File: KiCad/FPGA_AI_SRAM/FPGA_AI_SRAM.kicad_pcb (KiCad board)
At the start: 2 copper layers, 0 parts

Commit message: paddle schematic done
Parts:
- added C1: 0.1uF, Capacitor_SMD:C_0805_2012Metric, B.Cu at (130.8, 45.7)
- added J1: Conn_01x22_Male, Connector_PinHeader_2.54mm:PinHeader_1x22_P2.54mm_Vertical, F.Cu at (127.0, 59.7)
- added J2: Conn_01x22_Male, Connector_PinHeader_2.54mm:PinHeader_1x22_P2.54mm_Vertical, F.Cu at (134.6, 59.7)
- added U1: CY62157, Package_SO:TSOP-I-48_18.4x12mm_P0.5mm, F.Cu at (130.8, 45.7)

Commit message: possible pcb v1
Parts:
- C1: moved to F.Cu
- moved U1 45.4 mm to (110.5, 86.4)
- moved C1 36.9 mm to (106.7, 73.7)
- moved J1 25.4 mm to (101.6, 59.7)
- moved J2 15.2 mm to (119.4, 59.7)
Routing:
- net Net-(J1-Pad2): track 0.00 -> 60.4 mm
- net Net-(J2-Pad15): track 0.00 -> 57.0 mm
- net Net-(J1-Pad20): track 0.00 -> 44.0 mm
- net Net-(J2-Pad22): track 0.00 -> 40.4 mm, vias 0 -> 1
- net Net-(J1-Pad21): track 0.00 -> 40.1 mm, vias 0 -> 1
- net Net-(J1-Pad3): track 0.00 -> 37.5 mm, vias 0 -> 1
- net Net-(J2-Pad21): track 0.00 -> 37.2 mm, vias 0 -> 1
- net Net-(J1-Pad5): track 0.00 -> 36.3 mm, vias 0 -> 1
- net ~BLE: track 0.00 -> 36.1 mm
- net Net-(J2-Pad20): track 0.00 -> 35.6 mm, vias 0 -> 1
- net Net-(J1-Pad4): track 0.00 -> 34.5 mm, vias 0 -> 1
- net ~BHE: track 0.00 -> 33.5 mm
- net Net-(J2-Pad19): track 0.00 -> 32.4 mm, vias 0 -> 1
- net Net-(J2-Pad18): track 0.00 -> 30.3 mm, vias 0 -> 1
- net Net-(J1-Pad6): track 0.00 -> 29.0 mm, vias 0 -> 1
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- added copper zone on B.Cu, net GND
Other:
- board outline added: 22.9 x 58.4 mm
- board text added: "1 4"
- board text added: "10"
- board text added: "11"
- board text added: "12"
- board text added: "13"
- board text added: "3V3"
- board text added: "5"
- board text added: "6"
- board text added: "7"
- board text added: "8"
- board text added: "8Mbit SRAM"
- board text added: "9"
- board text added: "A0"
- board text added: "A1"
- board text added: "A15"
- board text added: "A16"
- board text added: "A17"
- board text added: "A18"
- board text added: "A19"
- board text added: "A2"
- board text added: "A3"
- board text added: "A4"
- board text added: "CE2"
- board text added: "D0"
- board text added: "D1"
- board text added: "D2"
- board text added: "D3"
- board text added: "D4"
- board text added: "D5"
- board text added: "D6"
- board text added: "GND"
- board text added: "~BHE"
- board text added: "~BLE"
- board text added: "~BYTE"
- board text added: "~CE1"
- board text added: "~OE"
- board text added: "~WE"

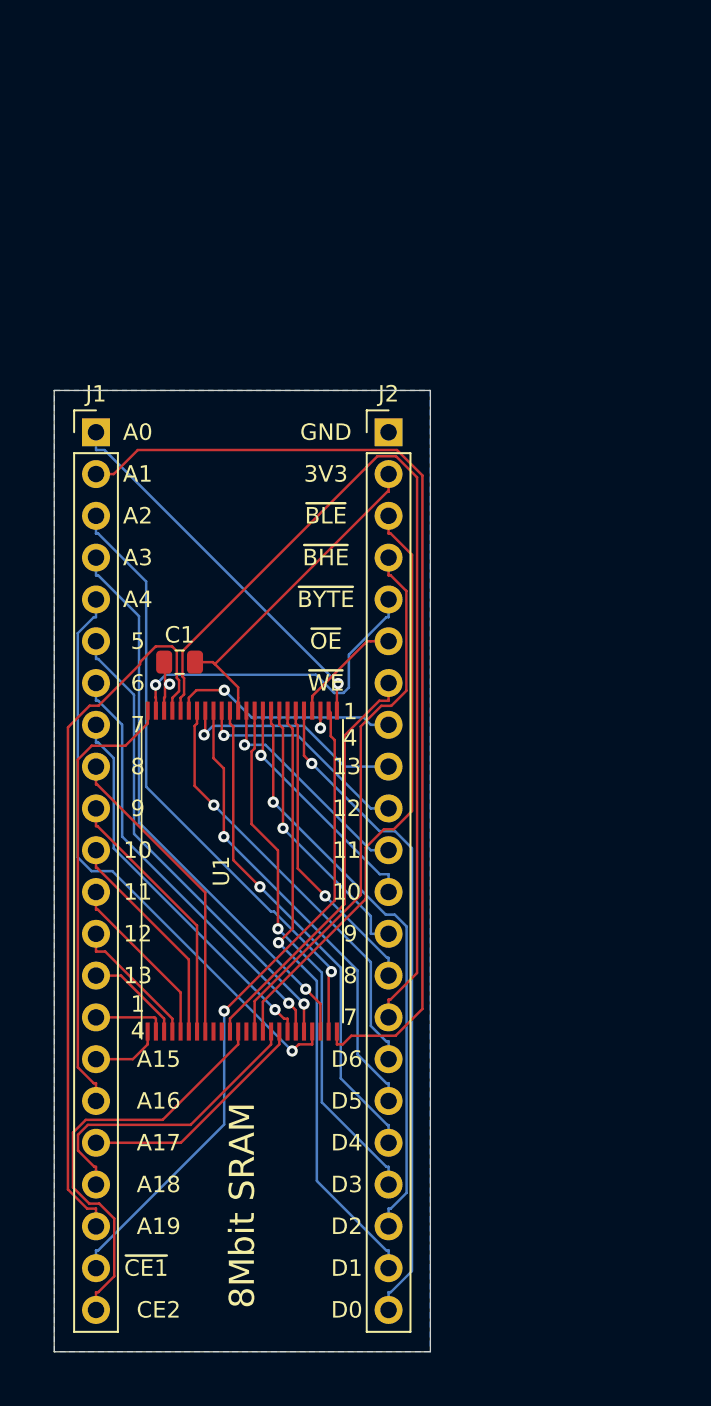
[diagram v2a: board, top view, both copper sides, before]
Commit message: better board with hand routed decoupler
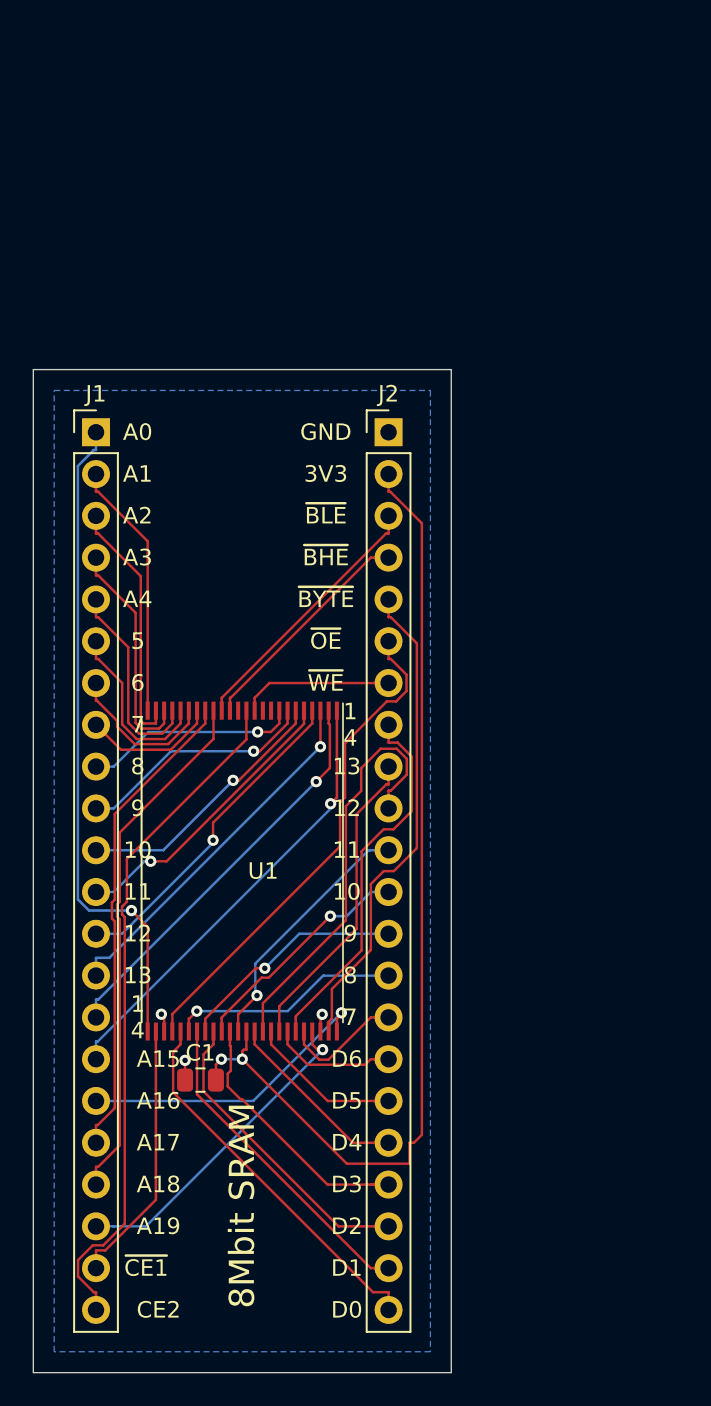
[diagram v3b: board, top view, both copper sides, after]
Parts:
- moved C1 25.4 mm to (108.0, 99.1)
- turned U1 to 270 degrees
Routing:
- net Net-(J2-Pad15): track 57.0 -> 7.37 mm
- net Net-(J1-Pad2): track 60.4 -> 15.8 mm
- net +3V3: track 20.6 -> 60.6 mm, vias 0 -> 2
- net Net-(J1-Pad20): track 44.0 -> 19.8 mm, vias 0 -> 1
- net Net-(J1-Pad5): track 36.3 -> 12.4 mm, vias 1 -> 0
- net Net-(J1-Pad21): track 40.1 -> 16.2 mm, vias 1 -> 0
- net ~OE: track 6.91 -> 30.5 mm
- net Net-(J1-Pad16): track 4.29 -> 27.3 mm, vias 0 -> 1
- net Net-(J1-Pad3): track 37.5 -> 15.4 mm, vias 1 -> 0
- net Net-(J1-Pad4): track 34.5 -> 13.9 mm, vias 1 -> 0
- net Net-(J1-Pad15): track 4.45 -> 24.6 mm, vias 0 -> 1
- net ~BLE: track 36.1 -> 16.1 mm
- net ~BHE: track 33.5 -> 13.9 mm
- net Net-(J2-Pad18): track 30.3 -> 11.4 mm, vias 1 -> 0
- net Net-(J2-Pad17): track 28.2 -> 9.34 mm, vias 1 -> 0
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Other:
- board size 22.9 x 58.4 mm -> 25.4 x 61 mm

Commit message: better board fully autorouted
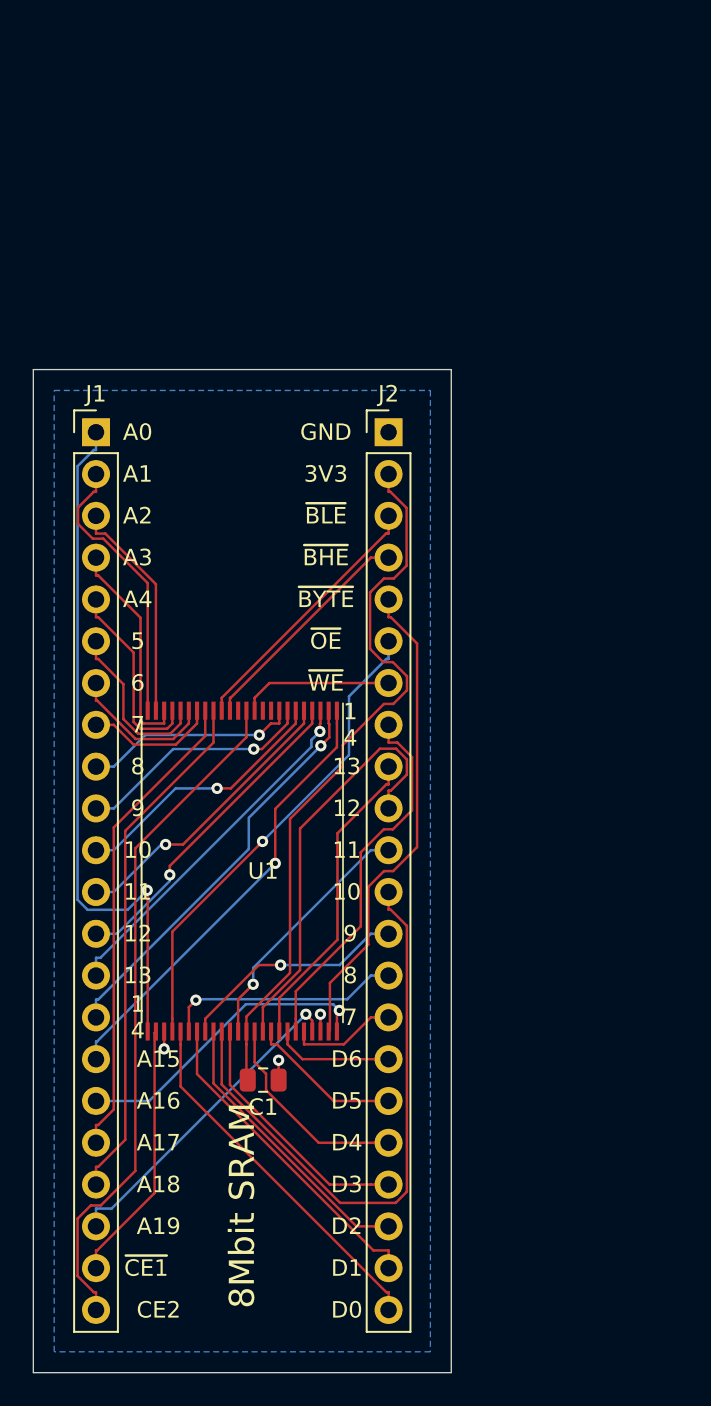
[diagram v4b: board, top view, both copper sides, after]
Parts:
- moved C1 3.81 mm to (111.8, 99.1), turned to 180 degrees
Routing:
- net Net-(J2-Pad12): track 14.2 -> 36.5 mm, vias 1 -> 0
- net +3V3: track 60.6 -> 44.3 mm, vias 2 -> 0
- net Net-(J1-Pad1): track 40.2 -> 42.5 mm
- net Net-(J1-Pad3): track 15.4 -> 13.7 mm
- net Net-(J2-Pad19): track 16.8 -> 15.4 mm
- net Net-(J1-Pad2): track 15.8 -> 17.0 mm
- net ~OE: track 30.5 -> 29.2 mm, vias 0 -> 1
- net Net-(J2-Pad18): track 11.4 -> 12.6 mm
- net Net-(J2-Pad20): track 18.5 -> 17.4 mm
- net Net-(J2-Pad22): track 23.1 -> 22.2 mm
- net Net-(J2-Pad15): track 7.37 -> 6.60 mm
- net Net-(J1-Pad4): track 13.9 -> 13.4 mm
- net Net-(J1-Pad6): track 10.9 -> 10.4 mm

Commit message: improved silkscreen, added 3d img
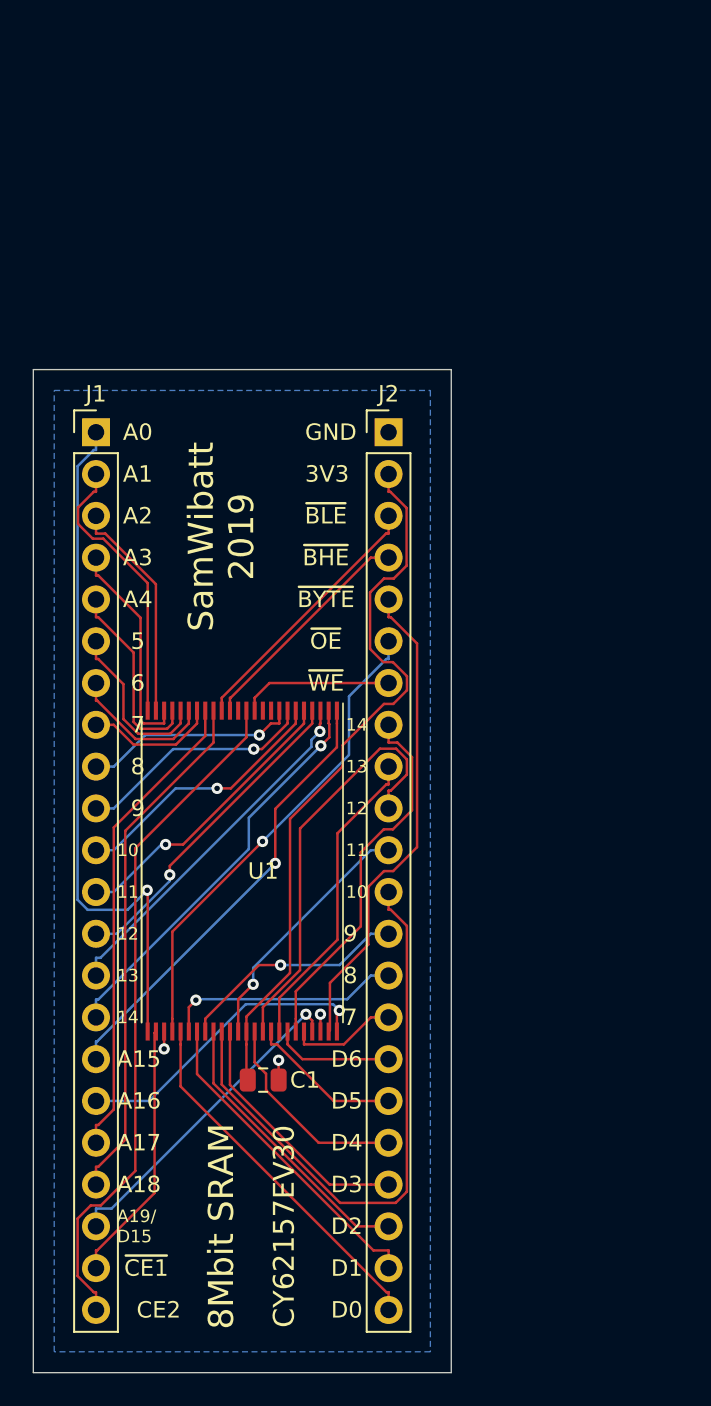
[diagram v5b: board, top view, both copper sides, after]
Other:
- board text added: "14"
- board text added: "A19/ D15"
- board text added: "CY62157EV30"
- board text added: "SamWibatt 2019"
- board text removed: "1 4"
- board text removed: "A19"
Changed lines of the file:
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@@
   (general
     (thickness 1.6)
-    (drawings 49)
+    (drawings 51)
     (tracks 309)
     (zones 0)
@@
     (tags capacitor)
     (attr smd)
-    (fp_text reference C1 (at 0 -1.65) (layer F.SilkS)
+    (fp_text reference C1 (at -2.54 0) (layer F.SilkS)
       (effects (font (size 1 1) (thickness 0.15)))
     )
@@
     )
   )
-  (gr_text "8Mbit SRAM" (at 110.49 106.68 90) (layer F.SilkS)
+  (gr_text "SamWibatt\n2019" (at 109.22 66.04 90) (layer F.SilkS)
+    (effects (font (size 1.524 1.524) (thickness 0.15)))
+  )
+  (gr_text CY62157EV30 (at 113.03 107.95 90) (layer F.SilkS)
+    (effects (font (size 1.27 1.27) (thickness 0.15)))
+  )
+  (gr_text "8Mbit SRAM" (at 109.22 107.95 90) (layer F.SilkS)
     (effects (font (size 1.524 1.524) (thickness 0.15)))
   )
@@
     (effects (font (size 1 1) (thickness 0.15)) (justify left))
   )
-  (gr_text "A19 " (at 105.41 107.95) (layer F.SilkS)
-    (effects (font (size 1 1) (thickness 0.15)))
-  )
-  (gr_text "A18 " (at 105.41 105.41) (layer F.SilkS)
-    (effects (font (size 1 1) (thickness 0.15)))
-  )
-  (gr_text "A17 " (at 105.41 102.87) (layer F.SilkS)
-    (effects (font (size 1 1) (thickness 0.15)))
-  )
-  (gr_text "A16 " (at 105.41 100.33) (layer F.SilkS)
-    (effects (font (size 1 1) (thickness 0.15)))
-  )
-  (gr_text "1 \n4 " (at 104.14 95.25) (layer F.SilkS)
-    (effects (font (size 1 1) (thickness 0.15)))
-  )
-  (gr_text "A15 " (at 105.41 97.79) (layer F.SilkS)
-    (effects (font (size 1 1) (thickness 0.15)))
-  )
-  (gr_text "13 " (at 104.14 92.71) (layer F.SilkS)
-    (effects (font (size 1 1) (thickness 0.15)))
-  )
-  (gr_text "12 " (at 104.14 90.17) (layer F.SilkS)
-    (effects (font (size 1 1) (thickness 0.15)))
-  )
-  (gr_text "11 " (at 104.14 87.63) (layer F.SilkS)
-    (effects (font (size 1 1) (thickness 0.15)))
-  )
-  (gr_text "10 " (at 104.14 85.09) (layer F.SilkS)
-    (effects (font (size 1 1) (thickness 0.15)))
+  (gr_text "A19/\nD15" (at 102.87 107.95) (layer F.SilkS)
+    (effects (font (size 0.762 0.762) (thickness 0.15)) (justify left))
+  )
+  (gr_text A18 (at 102.87 105.41) (layer F.SilkS)
+    (effects (font (size 1 1) (thickness 0.15)) (justify left))
+  )
+  (gr_text A17 (at 102.87 102.87) (layer F.SilkS)
+    (effects (font (size 1 1) (thickness 0.15)) (justify left))
+  )
+  (gr_text A16 (at 102.87 100.33) (layer F.SilkS)
+    (effects (font (size 1 1) (thickness 0.15)) (justify left))
+  )
+  (gr_text 14 (at 102.87 95.25) (layer F.SilkS)
+    (effects (font (size 0.762 0.762) (thickness 0.15)) (justify left))
+  )
+  (gr_text A15 (at 102.87 97.79) (layer F.SilkS)
+    (effects (font (size 1 1) (thickness 0.15)) (justify left))
+  )
+  (gr_text 13 (at 102.87 92.71) (layer F.SilkS)
+    (effects (font (size 0.762 0.762) (thickness 0.15)) (justify left))
+  )
+  (gr_text 12 (at 102.87 90.17) (layer F.SilkS)
+    (effects (font (size 0.762 0.762) (thickness 0.15)) (justify left))
+  )
+  (gr_text 11 (at 102.87 87.63) (layer F.SilkS)
+    (effects (font (size 0.762 0.762) (thickness 0.15)) (justify left))
+  )
+  (gr_text 10 (at 102.87 85.09) (layer F.SilkS)
+    (effects (font (size 0.762 0.762) (thickness 0.15)) (justify left))
   )
   (gr_text "9 " (at 104.14 82.55) (layer F.SilkS)
@@
     (effects (font (size 1 1) (thickness 0.15)))
   )
-  (gr_text " 1\n 4" (at 116.84 77.47) (layer F.SilkS)
-    (effects (font (size 1 1) (thickness 0.15)))
-  )
-  (gr_text 13 (at 116.84 80.01) (layer F.SilkS)
-    (effects (font (size 1 1) (thickness 0.15)))
-  )
-  (gr_text 12 (at 116.84 82.55) (layer F.SilkS)
-    (effects (font (size 1 1) (thickness 0.15)))
-  )
-  (gr_text 11 (at 116.84 85.09) (layer F.SilkS)
-    (effects (font (size 1 1) (thickness 0.15)))
-  )
-  (gr_text 10 (at 116.84 87.63) (layer F.SilkS)
-    (effects (font (size 1 1) (thickness 0.15)))
+  (gr_text 14 (at 118.11 77.47) (layer F.SilkS)
+    (effects (font (size 0.762 0.762) (thickness 0.15)) (justify right))
+  )
+  (gr_text 13 (at 118.11 80.01) (layer F.SilkS)
+    (effects (font (size 0.762 0.762) (thickness 0.15)) (justify right))
+  )
+  (gr_text 12 (at 118.11 82.55) (layer F.SilkS)
+    (effects (font (size 0.762 0.762) (thickness 0.15)) (justify right))
+  )
+  (gr_text 11 (at 118.11 85.09) (layer F.SilkS)
+    (effects (font (size 0.762 0.762) (thickness 0.15)) (justify right))
+  )
+  (gr_text 10 (at 118.11 87.63) (layer F.SilkS)
+    (effects (font (size 0.762 0.762) (thickness 0.15)) (justify right))
   )
   (gr_text " 9" (at 116.84 90.17) (layer F.SilkS)
@@
     (effects (font (size 1 1) (thickness 0.15)))
   )
-  (gr_text 3V3 (at 115.57 62.23) (layer F.SilkS)
-    (effects (font (size 1 1) (thickness 0.15)))
-  )
-  (gr_text GND (at 115.57 59.69) (layer F.SilkS)
-    (effects (font (size 1 1) (thickness 0.15)))
+  (gr_text 3V3 (at 114.3 62.23) (layer F.SilkS)
+    (effects (font (size 1 1) (thickness 0.15)) (justify left))
+  )
+  (gr_text GND (at 114.3 59.69) (layer F.SilkS)
+    (effects (font (size 1 1) (thickness 0.15)) (justify left))
   )
   (gr_line (start 97.79 116.84) (end 97.79 55.88) (layer Edge.Cuts) (width 0.05))

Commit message: added net names
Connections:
- net Net-(J1-Pad1) renamed /A0
- net Net-(J1-Pad10) renamed /A9
- net Net-(J1-Pad11) renamed /A10
- net Net-(J1-Pad12) renamed /A11
- net Net-(J1-Pad13) renamed /A12
- net Net-(J1-Pad14) renamed /A13
- net Net-(J1-Pad15) renamed /A14
- net Net-(J1-Pad16) renamed /A15
- net Net-(J1-Pad17) renamed /A16
- net Net-(J1-Pad18) renamed /A17
- net Net-(J1-Pad19) renamed /A18
- net Net-(J1-Pad2) renamed /A1
- net Net-(J1-Pad20) renamed /A19-IO15
- net Net-(J1-Pad21) renamed /~CE1
- net Net-(J1-Pad22) renamed /CE2
- net Net-(J1-Pad3) renamed /A2
- net Net-(J1-Pad4) renamed /A3
- net Net-(J1-Pad5) renamed /A4
- net Net-(J1-Pad6) renamed /A5
- net Net-(J1-Pad7) renamed /A6
- net Net-(J1-Pad8) renamed /A7
- net Net-(J1-Pad9) renamed /A8
- net Net-(J2-Pad10) renamed /IO12
- net Net-(J2-Pad11) renamed /IO11
- net Net-(J2-Pad12) renamed /IO10
- net Net-(J2-Pad13) renamed /IO9
- net Net-(J2-Pad14) renamed /IO8
- net Net-(J2-Pad15) renamed /IO7
- net Net-(J2-Pad16) renamed /IO6
- net Net-(J2-Pad17) renamed /IO5
- net Net-(J2-Pad18) renamed /IO4
- net Net-(J2-Pad19) renamed /IO3
- net Net-(J2-Pad20) renamed /IO2
- net Net-(J2-Pad21) renamed /I01
- net Net-(J2-Pad22) renamed /IO0
- net Net-(J2-Pad8) renamed /IO14
- net Net-(J2-Pad9) renamed /IO13
